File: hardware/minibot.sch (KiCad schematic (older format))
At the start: 36 parts

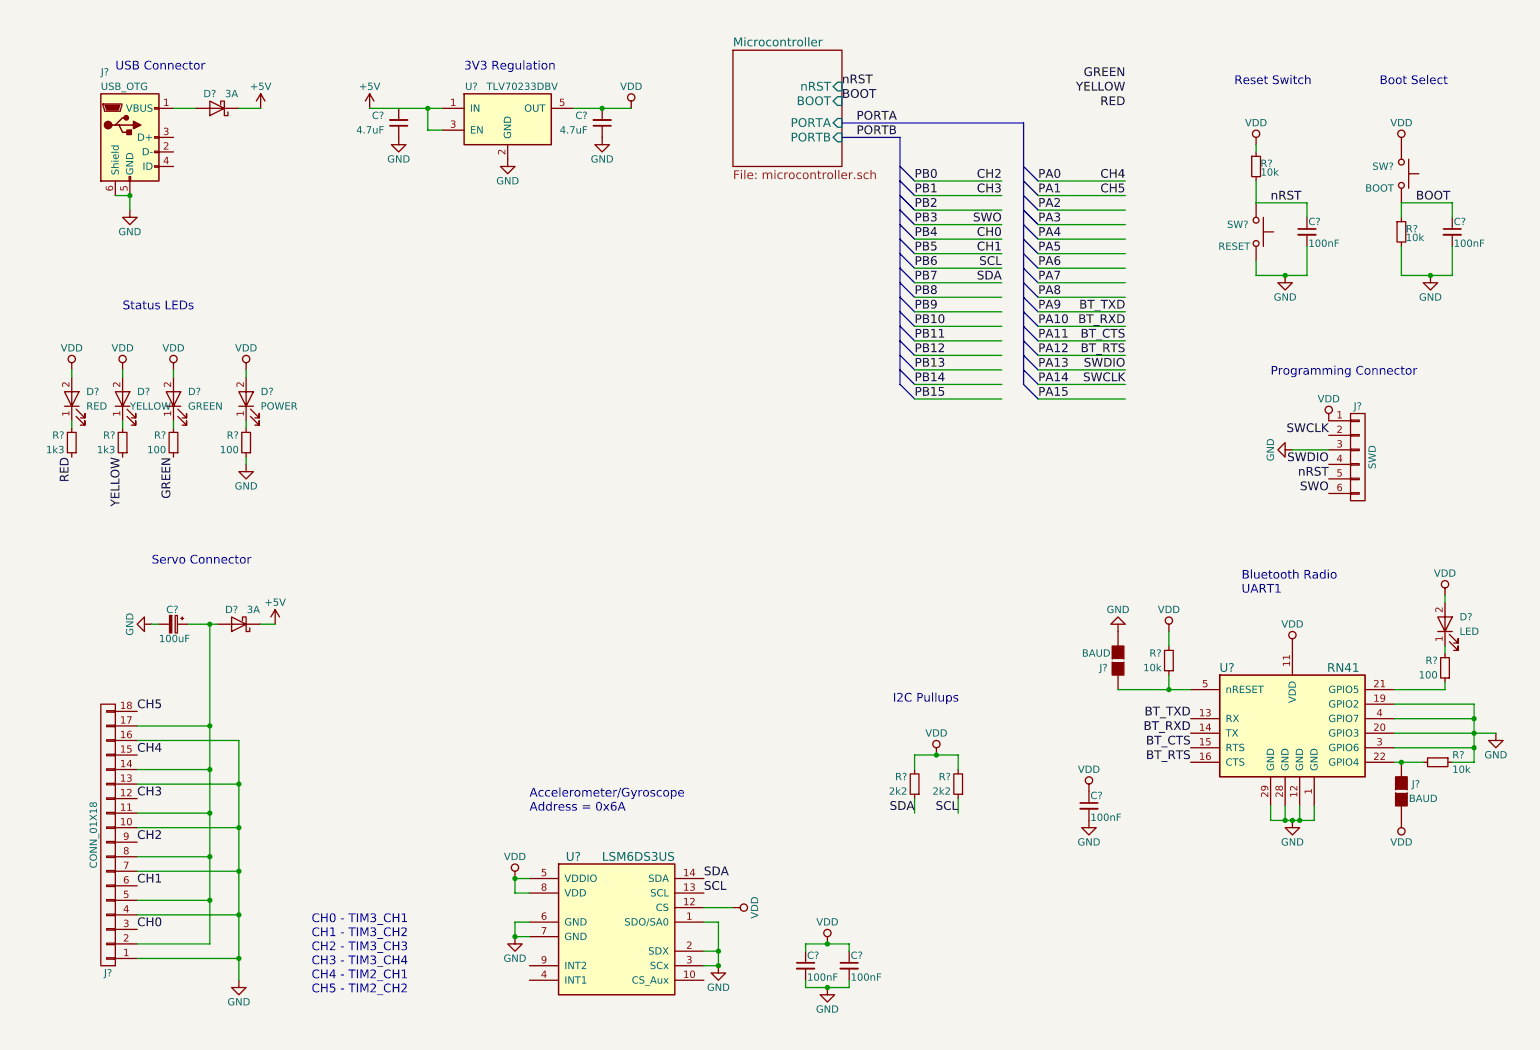
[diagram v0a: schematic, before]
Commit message: Map all of the inputs except for the debugging LEDs. Still need to work out how to deal with the camera.
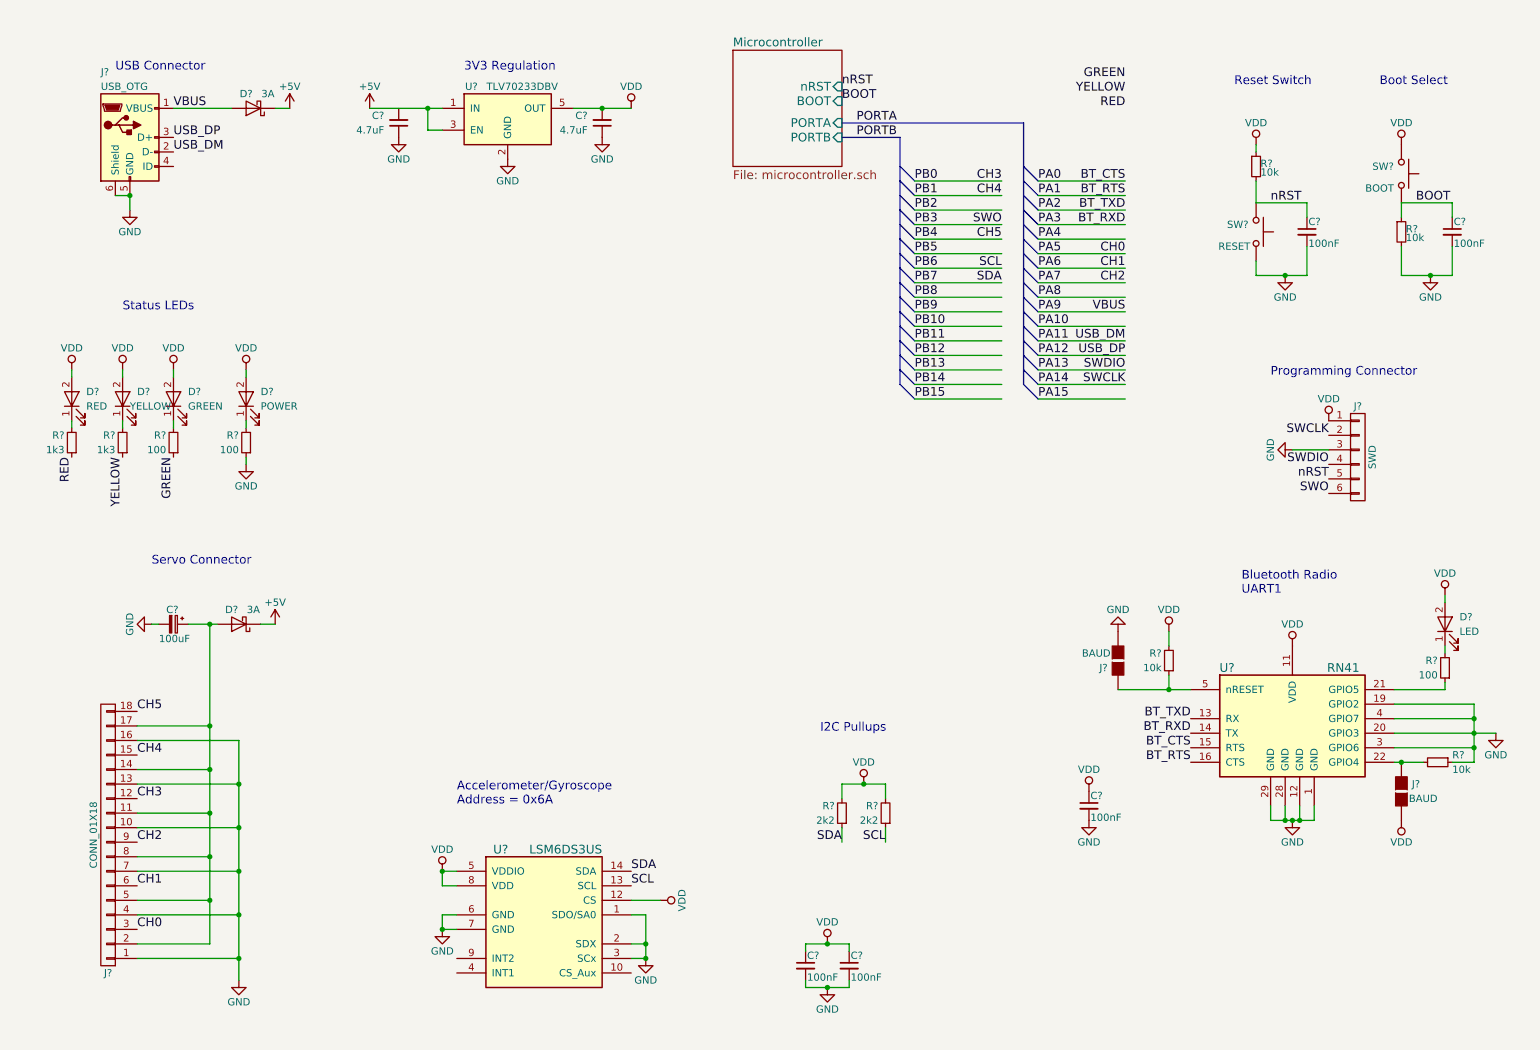
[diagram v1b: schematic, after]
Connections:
- net labels added: USB_DM, USB_DP, VBUS
- wire segments 122 -> 150
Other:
- note removed: "CH0 - TIM3_CH1\nCH1 - TIM3_CH2\nCH2 - TIM3_CH3\nCH3 - TIM3_CH4\nCH4 - TIM2_CH1\nCH5 - TIM2_CH2"
- moved on the sheet: D?, R?, U?

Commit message: Add the camera and finish off the schematic.
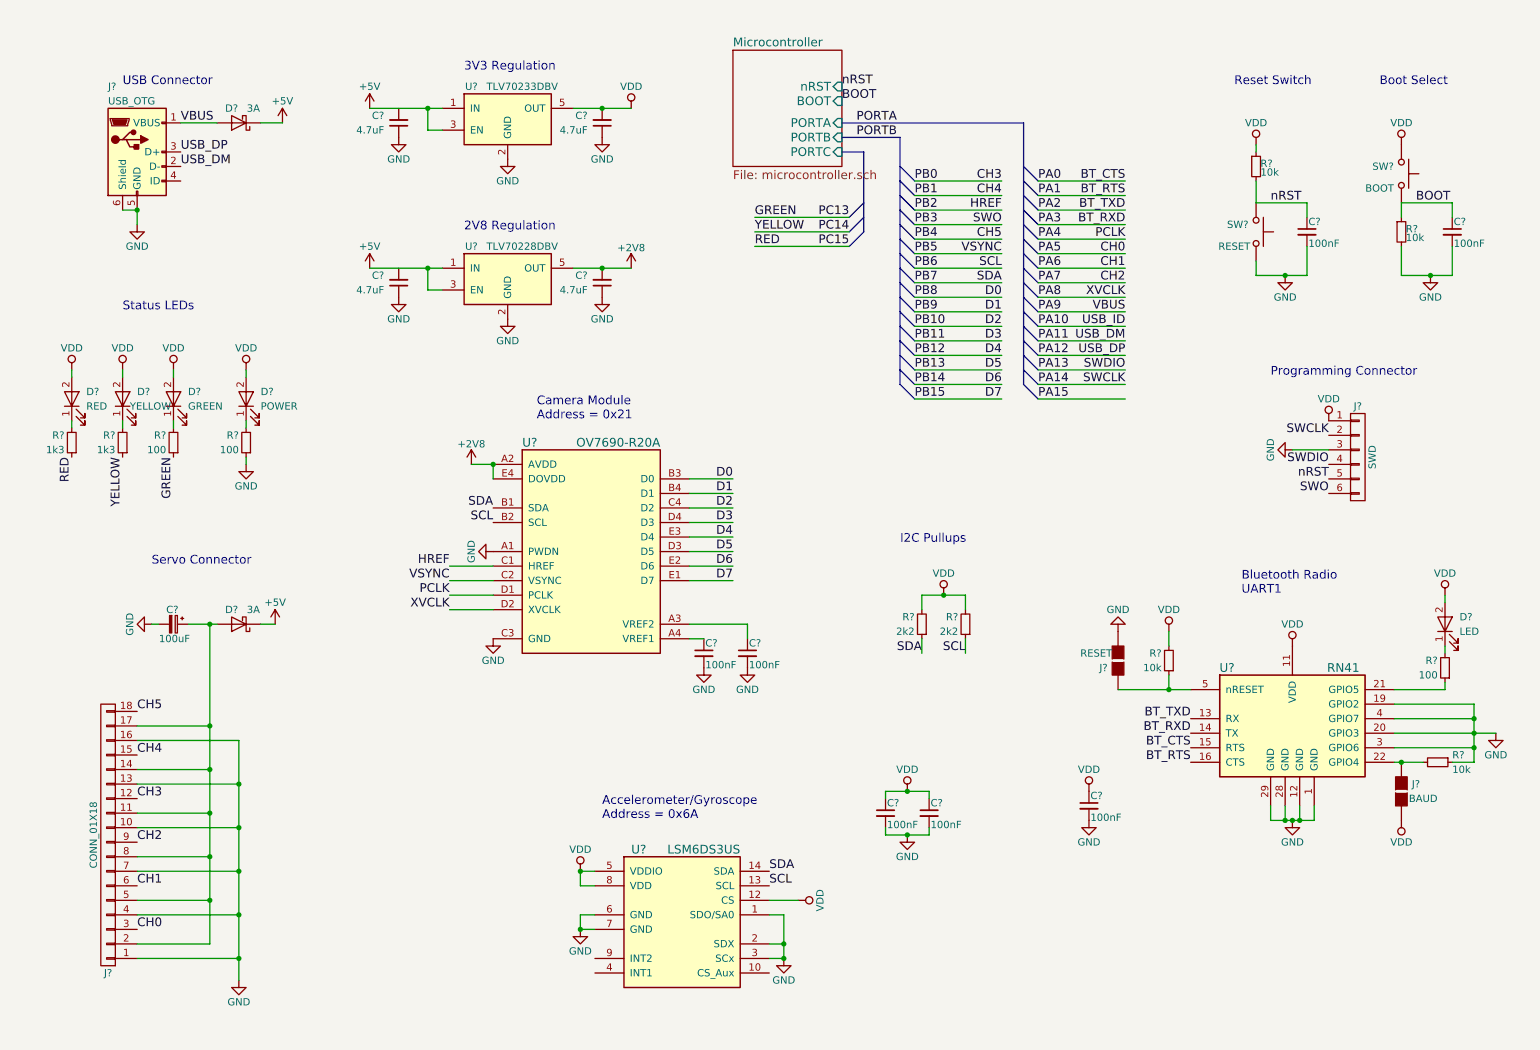
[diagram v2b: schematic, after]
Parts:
- added C? (x2): 4.7uF, symbol C_Small
- added C? (x2): 100nF, symbol C_Small
- added U?: OV7690-R20A, symbol OV7690-R20A
- added U?: TLV70228DBV, TO_SOT_Packages_SMD:SOT-23-5, symbol TLV70228DBV
- J?: value BAUD -> RESET
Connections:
- net labels added: +2V8, D0, D1, D2, D3, D4, D5, D6, D7, HREF, PC13, PC14, PC15, PCLK, USB_ID, VSYNC, XVCLK
- wire segments 150 -> 146
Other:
- note added: "2V8 Regulation\n"
- note added: "Camera Module\nAddress = 0x21\n"
- moved on the sheet: C?, D?, J?, R?, U?

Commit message: Fix the servo channels to ensure they use different PWM outputs. This required removing the flow control from the RN41 so CTS was tied to ground.
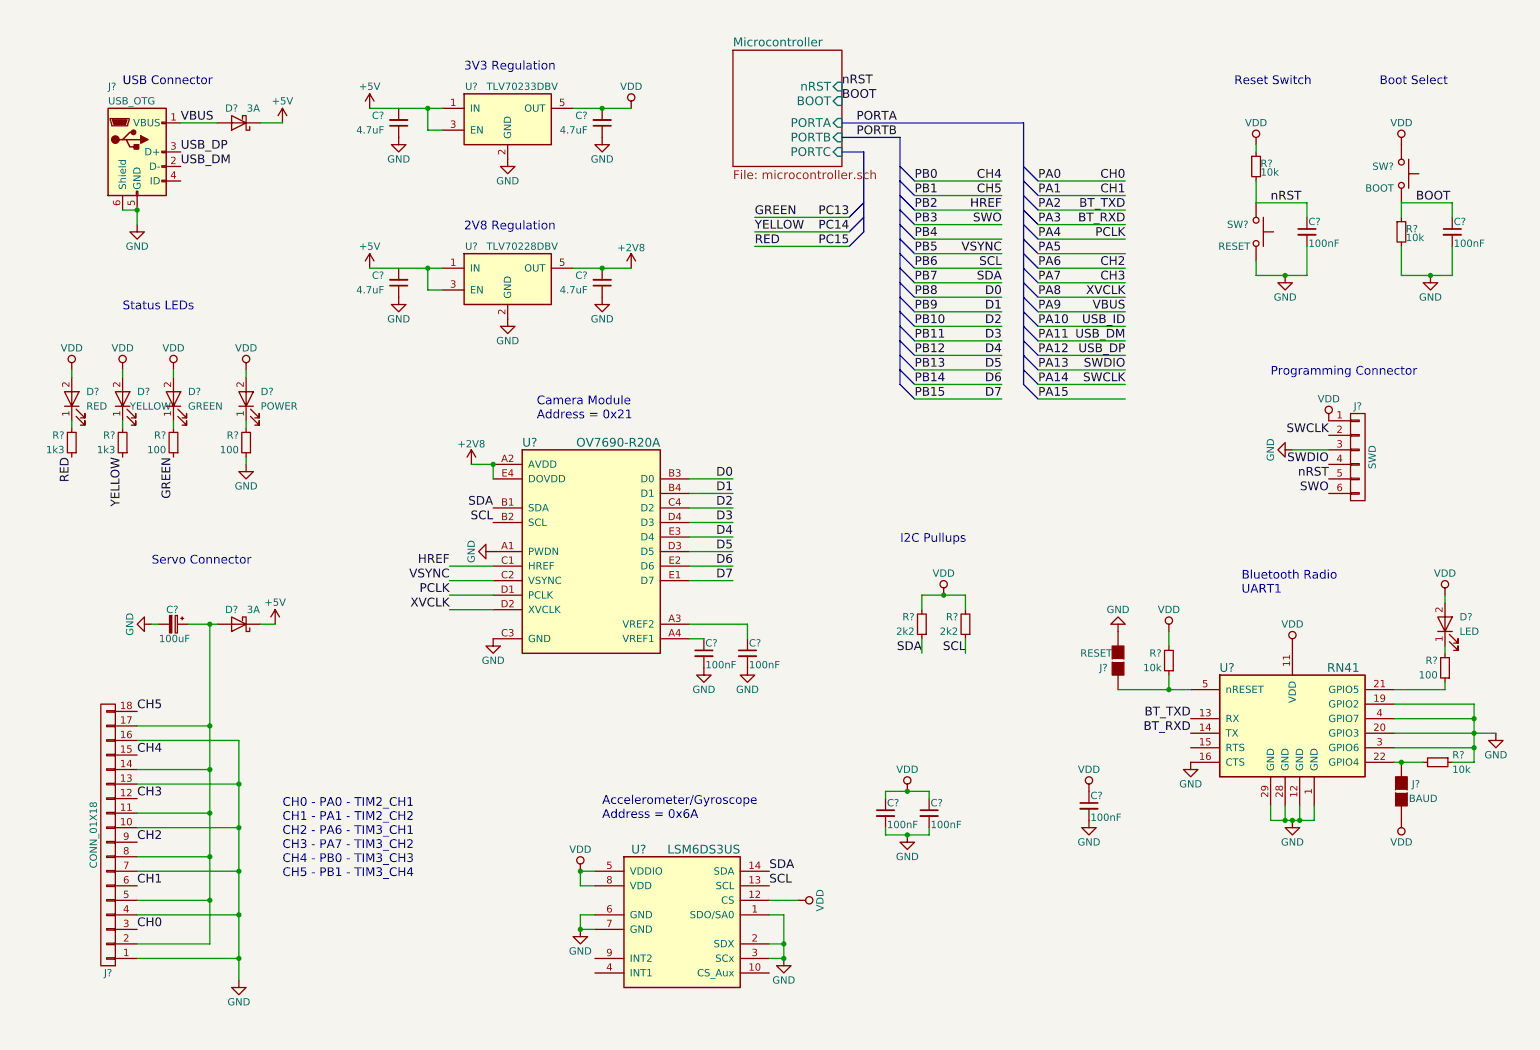
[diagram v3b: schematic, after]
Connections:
- net BT_RTS is gone; now on net GND: U?.16 (CTS)
- net BT_CTS: no longer names the net of U?.15 (RTS)
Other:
- note added: "CH0 - PA0 - TIM2_CH1\nCH1 - PA1 - TIM2_CH2\nCH2 - PA6 - TIM3_CH1\nCH3 - PA7 - TIM3_CH2\nCH4 - PB0 - TIM3_CH3\nCH5 - PB1 - TIM3_CH4"
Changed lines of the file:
@@
 Text Label 8750 5500 2    60   ~ 0
 BT_RXD
-Text Label 8750 5600 2    60   ~ 0
-BT_CTS
-Text Label 8750 5700 2    60   ~ 0
-BT_RTS
 Text Label 8300 1900 2    60   ~ 0
 BT_TXD
@@
 BT_RXD
 Text Label 8300 1700 2    60   ~ 0
-BT_CTS
+CH0
 Text Label 8300 1800 2    60   ~ 0
-BT_RTS
-Text Label 8300 2200 2    60   ~ 0
-CH0
+CH1
 Text Label 8300 2300 2    60   ~ 0
-CH1
+CH2
 Text Label 8300 2400 2    60   ~ 0
-CH2
+CH3
 Text Label 7450 1700 2    60   ~ 0
-CH3
+CH4
 Text Label 7450 1800 2    60   ~ 0
-CH4
-Text Label 7450 2100 2    60   ~ 0
 CH5
 $Comp
@@
 Text Notes 4250 3350 0    60   ~ 0
 Camera Module\nAddress = 0x21\n
+Text Notes 2500 6500 0    60   ~ 0
+CH0 - PA0 - TIM2_CH1\nCH1 - PA1 - TIM2_CH2\nCH2 - PA6 - TIM3_CH1\nCH3 - PA7 - TIM3_CH2\nCH4 - PB0 - TIM3_CH3\nCH5 - PB1 - TIM3_CH4
+$Comp
+L GND #PWR?
+U 1 1 5949392F
+P 8750 5700
+F 0 "#PWR?" H 8750 5450 50  0001 C CNN
+F 1 "GND" H 8750 5550 50  0000 C CNN
+F 2 "" H 8750 5700 50  0001 C CNN
+F 3 "" H 8750 5700 50  0001 C CNN
+	1    8750 5700
+	1    0    0    -1
+$EndComp
 $EndSCHEMATC

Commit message: Add missing camera decoupling. Annotate all parts.
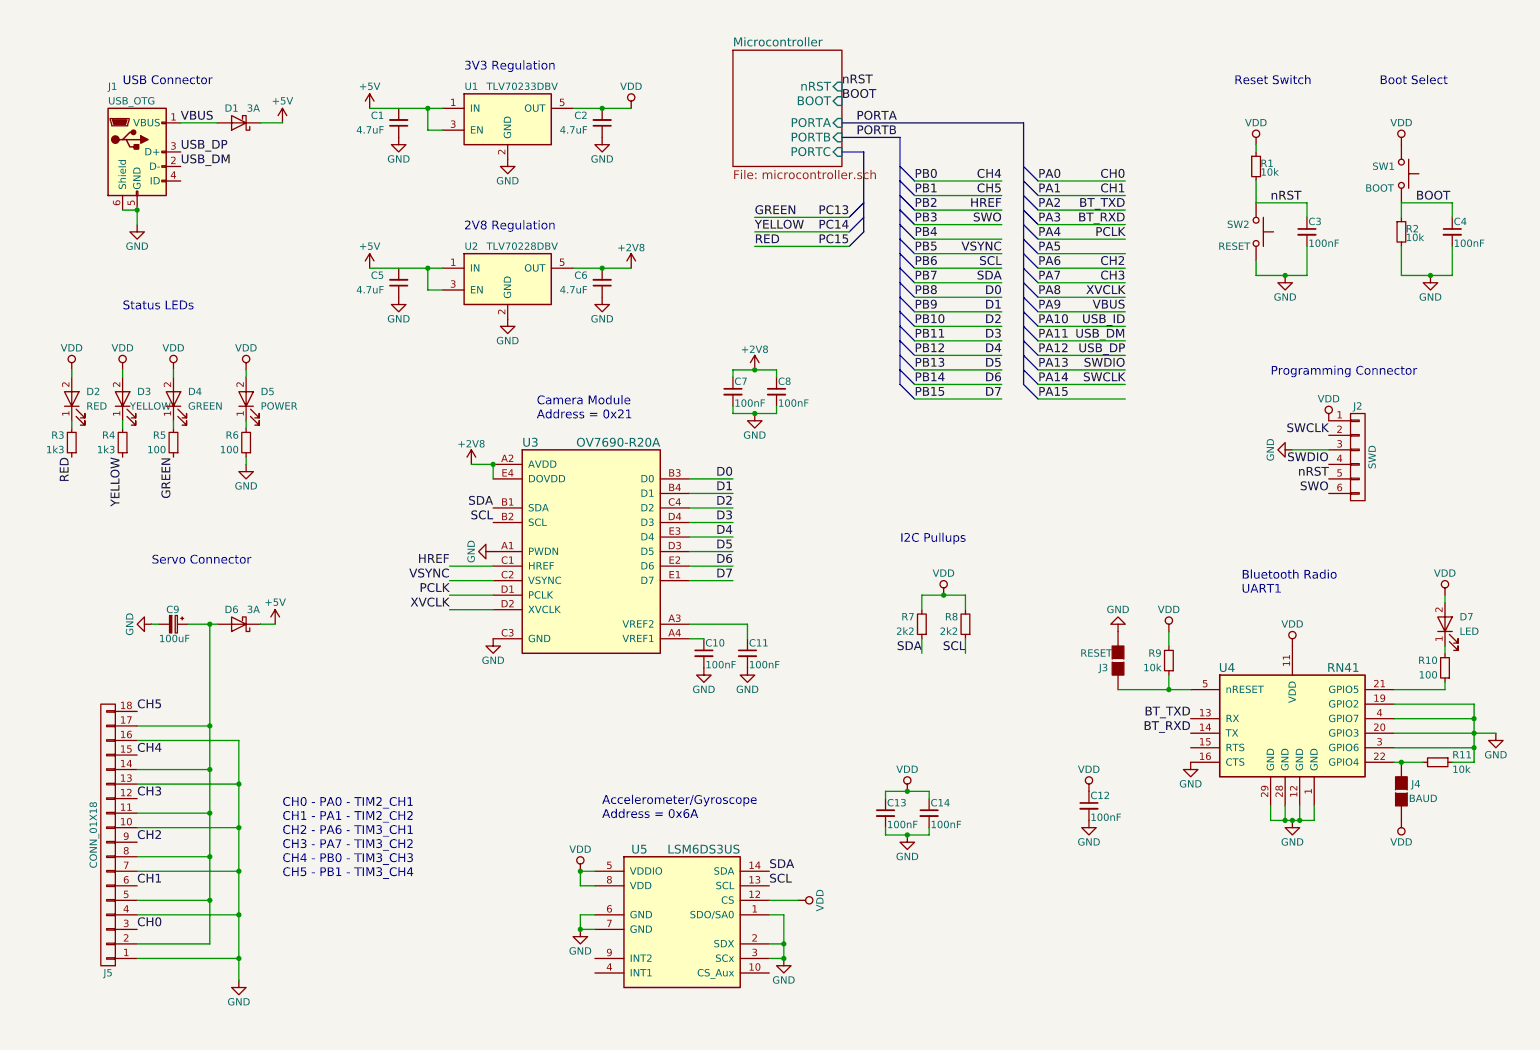
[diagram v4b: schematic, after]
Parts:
- added C7, C8: 100nF, symbol C_Small
- gave numbers to parts that had none: 42
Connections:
- net +2V8: now also C7.1, C8.1
- net GND: now also C7.2, C8.2

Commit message: Associate the simple parts with footprints. Some custom footprints will need to be designed.
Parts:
- C1, C2, C5, C6: footprint (none) -> Capacitors_SMD:C_0805
- C10, C11, C12, C13, C14, C3, C4, C7, C8: footprint (none) -> Capacitors_SMD:C_0603
- C9: footprint (none) -> Capacitors_SMD:CP_Elec_6.3x5.3
- D1, D6: footprint (none) -> Diodes_SMD:D_SMA
- D2, D3, D4, D5, D7: footprint (none) -> LEDs:LED_0603
- J1: footprint (none) -> Connectors:USB_Micro-B
- J2: footprint (none) -> Pin_Headers:Pin_Header_Angled_1x06_Pitch1.27mm
- R1, R10, R11, R2, R3, R4, R5, R6, R7, R8, R9: footprint (none) -> Resistors_SMD:R_0603
